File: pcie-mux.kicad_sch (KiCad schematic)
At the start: 50 parts, among them Q6 BSS138PW,115, Q7 BSS138PW,115, Q8 BSS138PW,115, SW1 SW_CVS-02B, U10 TMUXHS4412RUAR, U11 CBTL02043ABQ, U7 SY75602BTWL-TR, U8 74LVC1G157-Q100H_SOT457, U9 NTS0302JKZ

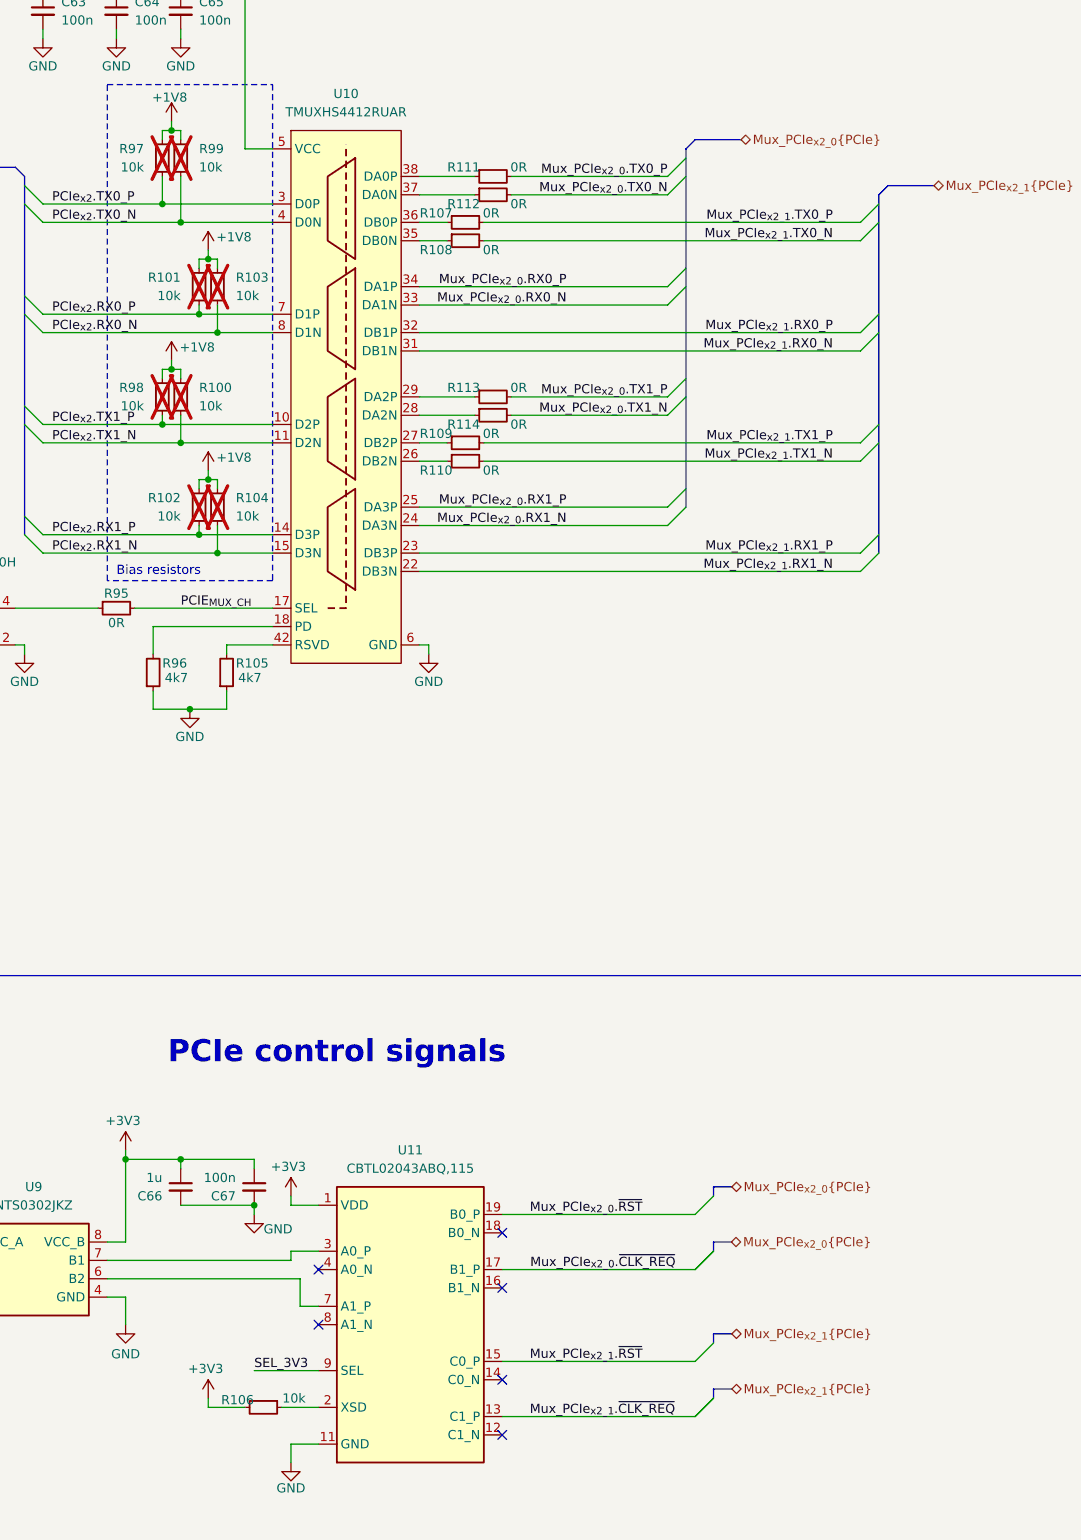
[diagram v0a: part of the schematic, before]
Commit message: [#100765] Prettify schematic
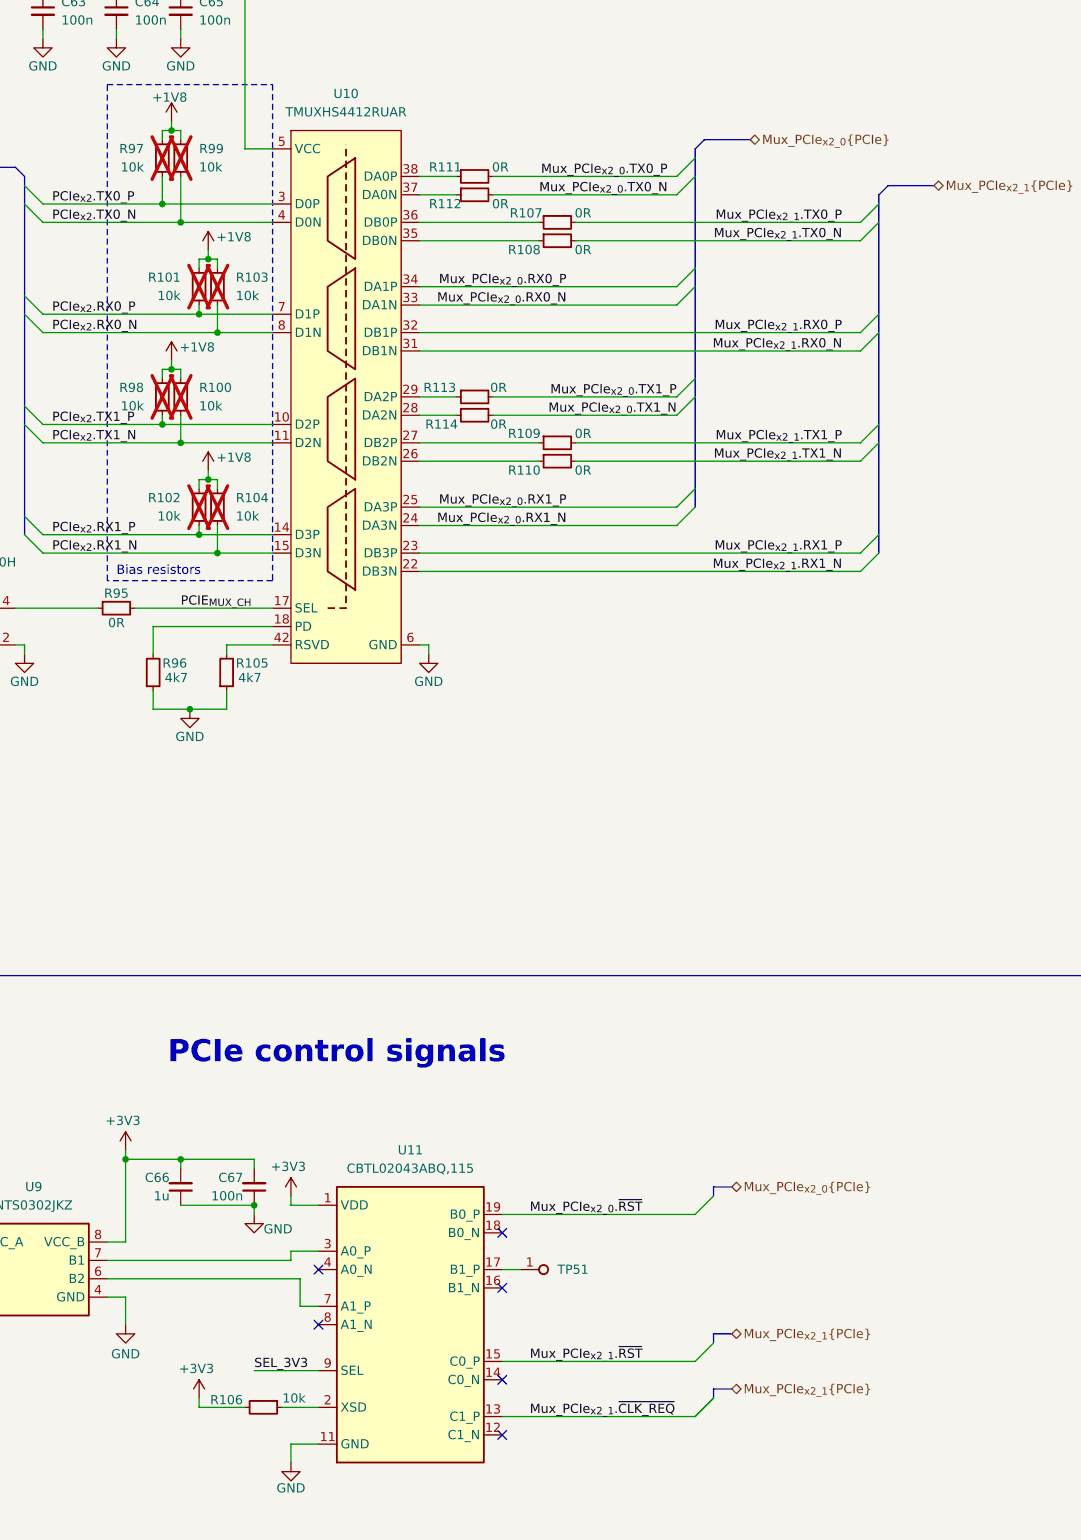
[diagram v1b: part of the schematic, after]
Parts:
- added TP51: TP_1mm_SMD, antmicro-footprints:TP_SMD_1mm, symbol antmicroTestPoints:TP_1mm_SMD
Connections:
- net +3V3: now also C66.2, C67.2; no longer C66.1, C67.1
- net GND: now also C66.1, C67.1; no longer C66.2, C67.2
- net Mux_PCIe_{x2_0}.~{CLK_REQ}: no longer names the net of U11.17 (B1_P)
- net Mux_PCIe_{x2_0}.~{CLK_REQ}: now also TP51.1
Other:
- moved on the sheet: R107, R108, R109, R110, R111, R112, R113, R114

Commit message: [#101557] Fix designator in status LED label
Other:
- note added: "D8: OFF, D9: ON = PORT A"
- note added: "D8: ON, D9: OFF = PORT B"
- note removed: "D6: OFF, D7: ON = PORT A"
- note removed: "D6: ON, D7: OFF = PORT B"
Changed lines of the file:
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@@
 		)
 	)
-	(text "D6: OFF, D7: ON = PORT A"
+	(text "D8: OFF, D9: ON = PORT A"
 		(exclude_from_sim no)
 		(at 107.188 211.074 0)
@@
 		)
 	)
-	(text "D6: ON, D7: OFF = PORT B"
+	(text "D8: ON, D9: OFF = PORT B"
 		(exclude_from_sim no)
 		(at 93.98 214.63 0)

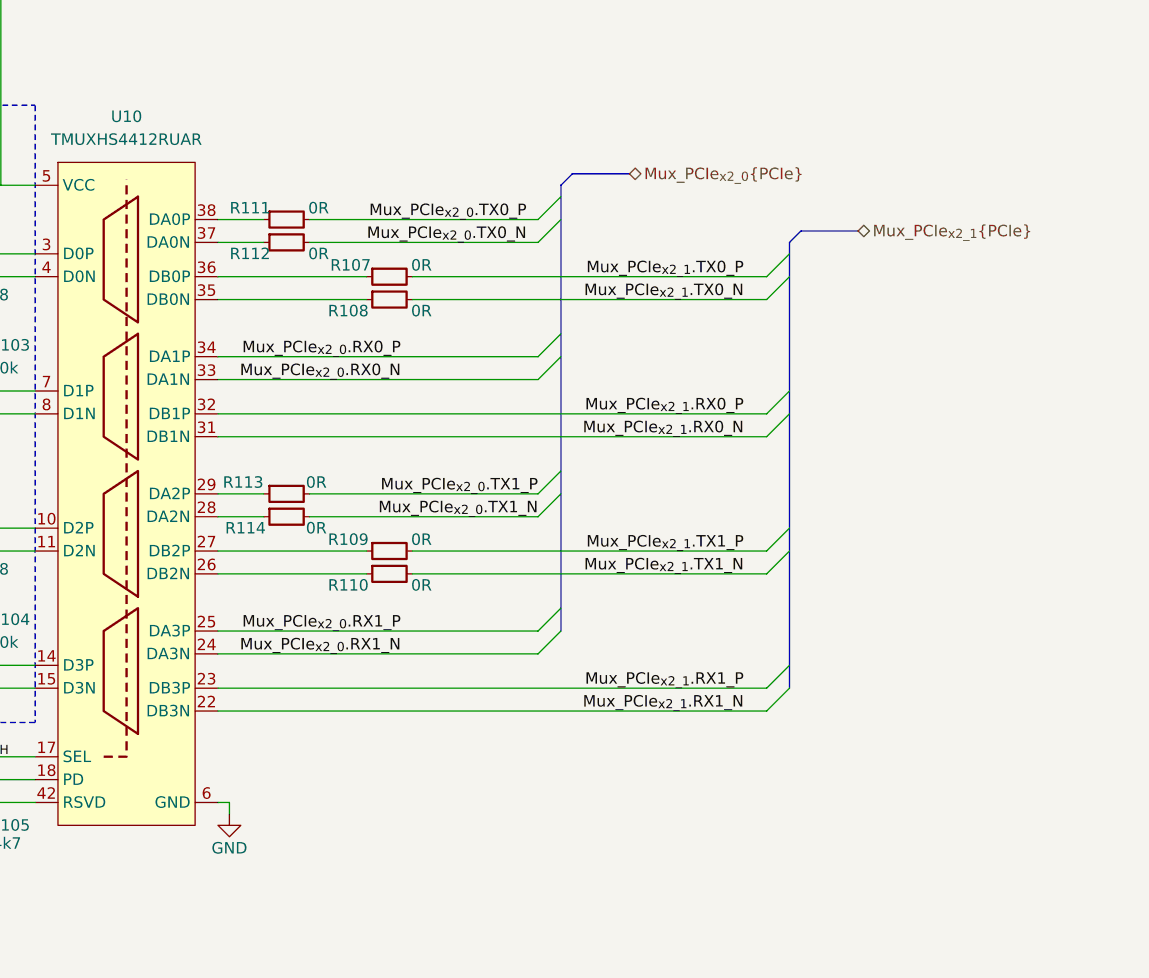
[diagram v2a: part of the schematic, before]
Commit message: [#101557] Add additional labels on HS lines
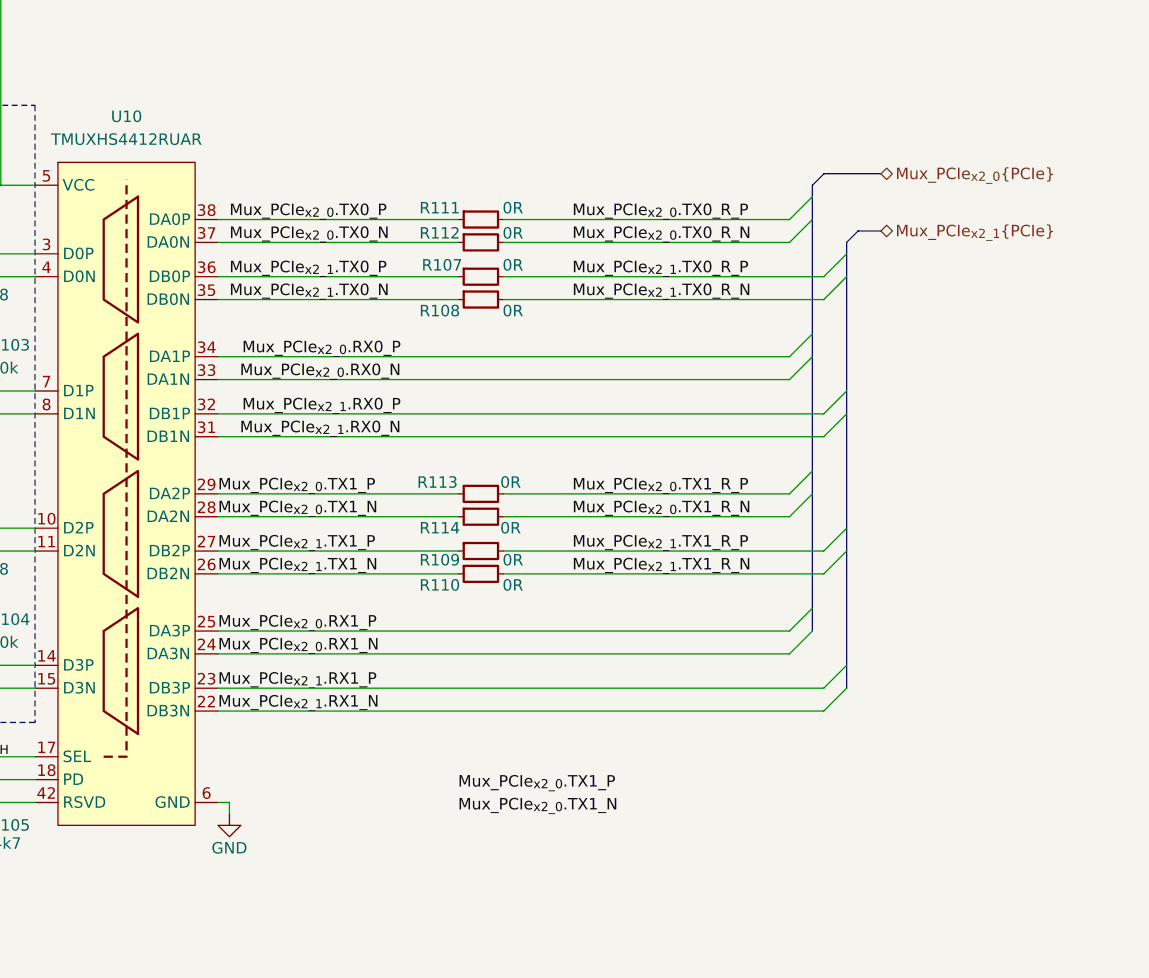
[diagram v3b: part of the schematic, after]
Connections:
- net Mux_PCIe_{x2_0}.TX0_N: now also R112.1, U10.37 (DA0N); no longer R112.2
- net Mux_PCIe_{x2_0}.TX0_P: now also R111.1, U10.38 (DA0P); no longer R111.2
- net Mux_PCIe_{x2_0}.TX1_N: now also R114.1, U10.28 (DA2N); no longer R114.2
- net Mux_PCIe_{x2_0}.TX1_P: now also R113.1, U10.29 (DA2P); no longer R113.2
- net Mux_PCIe_{x2_1}.TX0_N: now also R108.1, U10.35 (DB0N); no longer R108.2
- net Mux_PCIe_{x2_1}.TX0_P: now also R107.1, U10.36 (DB0P); no longer R107.2
- net Mux_PCIe_{x2_1}.TX1_N: now also R110.1, U10.26 (DB2N); no longer R110.2
- net Mux_PCIe_{x2_1}.TX1_P: now also R109.1, U10.27 (DB2P); no longer R109.2
- new net Mux_PCIe_{x2_0}.TX0_R_N: R112.2
- new net Mux_PCIe_{x2_0}.TX0_R_P: R111.2
- new net Mux_PCIe_{x2_0}.TX1_R_N: R114.2
- new net Mux_PCIe_{x2_0}.TX1_R_P: R113.2
- new net Mux_PCIe_{x2_1}.TX0_R_N: R108.2
- new net Mux_PCIe_{x2_1}.TX0_R_P: R107.2
- new net Mux_PCIe_{x2_1}.TX1_R_N: R110.2
- new net Mux_PCIe_{x2_1}.TX1_R_P: R109.2
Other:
- moved on the sheet: R107, R108, R109, R110, R111, R112, R113, R114

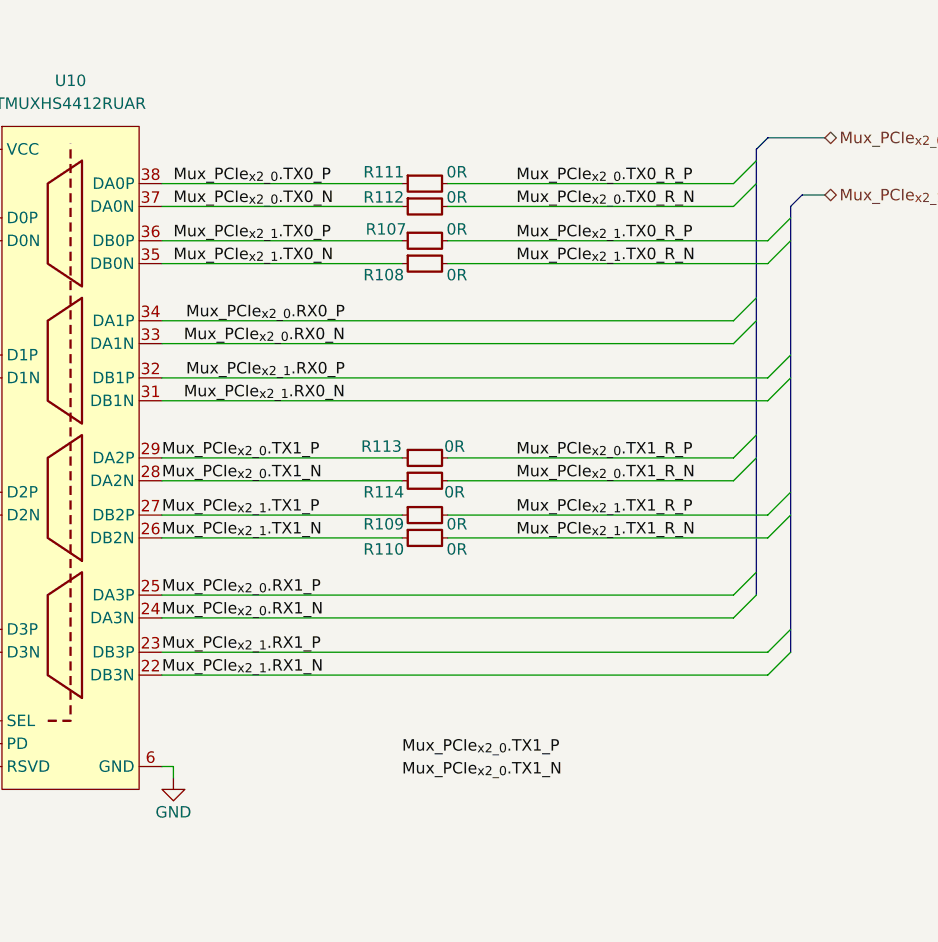
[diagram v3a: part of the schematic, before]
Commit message: [#101859] Add HS fanout from connectors
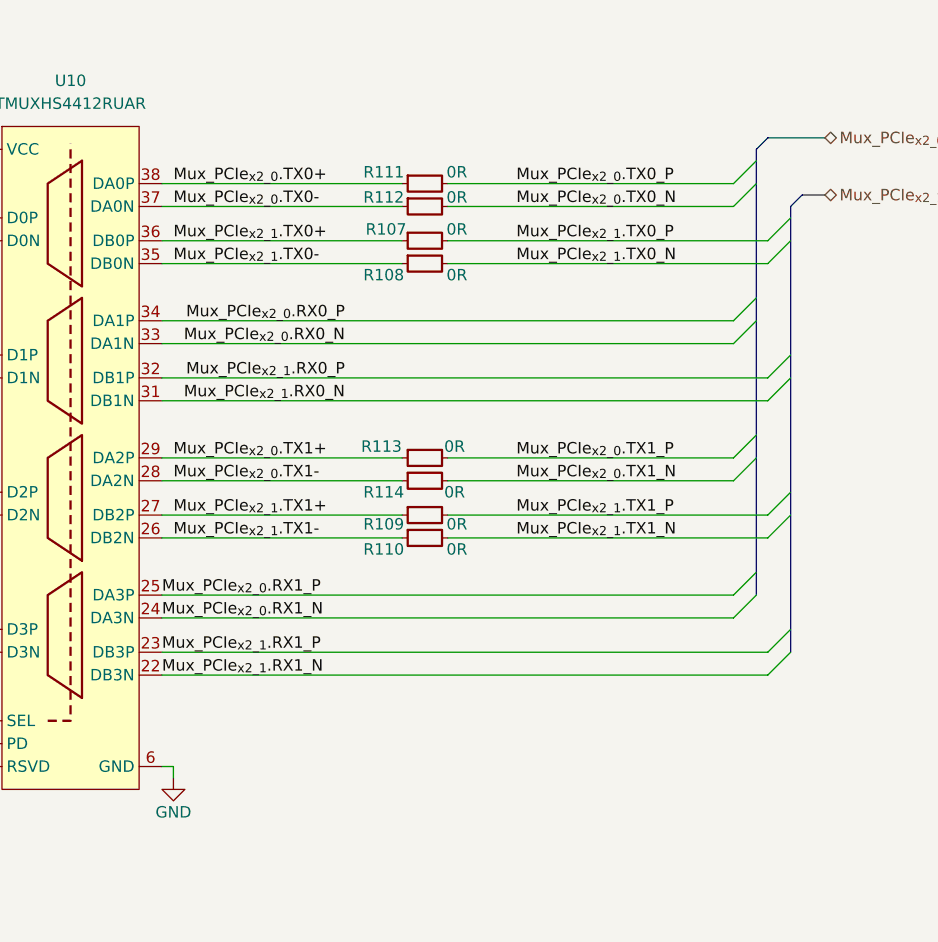
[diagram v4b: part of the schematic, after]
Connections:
- net Mux_PCIe_{x2_0}.TX0_R_N is gone; now on net Mux_PCIe_{x2_0}.TX0_N: R112.2
- net Mux_PCIe_{x2_0}.TX0_R_P is gone; now on net Mux_PCIe_{x2_0}.TX0_P: R111.2
- net Mux_PCIe_{x2_0}.TX1_R_N is gone; now on net Mux_PCIe_{x2_0}.TX1_N: R114.2
- net Mux_PCIe_{x2_0}.TX1_R_P is gone; now on net Mux_PCIe_{x2_0}.TX1_P: R113.2
- net Mux_PCIe_{x2_1}.TX0_R_N is gone; now on net Mux_PCIe_{x2_1}.TX0_N: R108.2
- net Mux_PCIe_{x2_1}.TX0_R_P is gone; now on net Mux_PCIe_{x2_1}.TX0_P: R107.2
- net Mux_PCIe_{x2_1}.TX1_R_N is gone; now on net Mux_PCIe_{x2_1}.TX1_N: R110.2
- net Mux_PCIe_{x2_1}.TX1_R_P is gone; now on net Mux_PCIe_{x2_1}.TX1_P: R109.2
- net Mux_PCIe_{x2_0}.TX0_N: no longer R112.1, U10.37 (DA0N)
- net Mux_PCIe_{x2_0}.TX0_P: no longer R111.1, U10.38 (DA0P)
- net Mux_PCIe_{x2_0}.TX1_N: no longer R114.1, U10.28 (DA2N)
- net Mux_PCIe_{x2_0}.TX1_P: no longer R113.1, U10.29 (DA2P)
- net Mux_PCIe_{x2_1}.TX0_N: no longer R108.1, U10.35 (DB0N)
- net Mux_PCIe_{x2_1}.TX0_P: no longer R107.1, U10.36 (DB0P)
- net Mux_PCIe_{x2_1}.TX1_N: no longer R110.1, U10.26 (DB2N)
- net Mux_PCIe_{x2_1}.TX1_P: no longer R109.1, U10.27 (DB2P)
- new net Mux_PCIe_{x2_0}.TX0+: R111.1, U10.38 (DA0P)
- new net Mux_PCIe_{x2_0}.TX0-: R112.1, U10.37 (DA0N)
- new net Mux_PCIe_{x2_0}.TX1+: R113.1, U10.29 (DA2P)
- new net Mux_PCIe_{x2_0}.TX1-: R114.1, U10.28 (DA2N)
- new net Mux_PCIe_{x2_1}.TX0+: R107.1, U10.36 (DB0P)
- new net Mux_PCIe_{x2_1}.TX0-: R108.1, U10.35 (DB0N)
- new net Mux_PCIe_{x2_1}.TX1+: R109.1, U10.27 (DB2P)
- new net Mux_PCIe_{x2_1}.TX1-: R110.1, U10.26 (DB2N)
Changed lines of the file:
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@@
-		)
-	)
-	(label "Mux_PCIe_{x2_0}.TX0_R_P"
-		(at 353.06 67.31 0)
-		(effects
-			(font
-				(size 1.27 1.27)
-			)
-			(justify left bottom)
 		)
 	)
@@
 		)
 	)
-	(label "Mux_PCIe_{x2_0}.TX1_P"
-		(at 340.36 130.81 0)
-		(effects
-			(font
-				(size 1.27 1.27)
-			)
-			(justify left bottom)
-		)
-	)
 	(label "Mux_PCIe_{x2_1}.TX1_N"
-		(at 313.69 106.68 0)
+		(at 353.06 106.68 0)
 		(effects
 			(font
@@
 		)
 	)
-	(label "Mux_PCIe_{x2_0}.TX0_R_N"
-		(at 353.06 69.85 0)
-		(effects
-			(font
-				(size 1.27 1.27)
-			)
-			(justify left bottom)
-		)
-	)
 	(label "Mux_PCIe_{x2_0}.RX0_N"
 		(at 334.01 85.09 180)
@@
 		)
 	)
+	(label "Mux_PCIe_{x2_1}.TX0+"
+		(at 314.96 73.66 0)
+		(effects
+			(font
+				(size 1.27 1.27)
+			)
+			(justify left bottom)
+		)
+	)
 	(label "PCIe_{x2}.~{RST}"
 		(at 220.98 217.17 180)
@@
 	)
 	(label "Mux_PCIe_{x2_0}.TX1_P"
-		(at 313.69 97.79 0)
+		(at 353.06 97.79 0)
 		(effects
 			(font
@@
 	)
 	(label "Mux_PCIe_{x2_1}.TX0_P"
-		(at 314.96 73.66 0)
+		(at 353.06 73.66 0)
 		(effects
 			(font
@@
 	)
 	(label "Mux_PCIe_{x2_1}.TX0_N"
-		(at 314.96 76.2 0)
+		(at 353.06 76.2 0)
 		(effects
 			(font
@@
 	)
 	(label "Mux_PCIe_{x2_0}.TX1_N"
-		(at 313.69 100.33 0)
+		(at 353.06 100.33 0)
 		(effects
 			(font
@@
 	)
 	(label "Mux_PCIe_{x2_0}.TX0_N"
-		(at 314.96 69.85 0)
+		(at 353.06 69.85 0)
 		(effects
 			(font
@@
 		)
 	)
+	(label "Mux_PCIe_{x2_0}.TX0+"
+		(at 314.96 67.31 0)
+		(effects
+			(font
+				(size 1.27 1.27)
+			)
+			(justify left bottom)
+		)
+	)
 	(label "PCIe_{x2}.TX1_P"
 		(at 262.89 101.6 0)
@@
 	)
 	(label "Mux_PCIe_{x2_1}.TX1_P"
-		(at 313.69 104.14 0)
+		(at 353.06 104.14 0)
 		(effects
 			(font
@@
 		)
 	)
-	(label "Mux_PCIe_{x2_1}.TX0_R_P"
-		(at 353.06 73.66 0)
-		(effects
-			(font
-				(size 1.27 1.27)
-			)
-			(justify left bottom)
-		)
-	)
 	(label "Mux_PCIe_{x2_1}.CLK_N"
 		(at 100.33 143.51 0)
@@
 		)
 	)
-	(label "Mux_PCIe_{x2_1}.TX1_R_P"
-		(at 353.06 104.14 0)
+	(label "Mux_PCIe_{x2_0}.TX1-"
+		(at 314.96 100.33 0)
 		(effects
 			(font
@@
 		)
 	)
-	(label "Mux_PCIe_{x2_0}.TX1_N"
-		(at 340.36 133.35 0)
-		(effects
-			(font
-				(size 1.27 1.27)
-			)
-			(justify left bottom)
-		)
-	)
-	(label "Mux_PCIe_{x2_0}.TX1_R_P"
-		(at 353.06 97.79 0)
-		(effects
-			(font
-				(size 1.27 1.27)
-			)
-			(justify left bottom)
-		)
-	)
-	(label "Mux_PCIe_{x2_1}.TX0_R_N"
-		(at 353.06 76.2 0)
-		(effects
-			(font
-				(size 1.27 1.27)
-			)
-			(justify left bottom)
-		)
-	)
 	(label "Mux_PCIe_{x2_1}.~{CLK_REQ}"
 		(at 328.93 238.76 0)
@@
 		)
 	)
-	(label "Mux_PCIe_{x2_0}.TX1_R_N"
-		(at 353.06 100.33 0)
+	(label "Mux_PCIe_{x2_1}.TX1-"
+		(at 314.96 106.68 0)
 		(effects
 			(font
@@
 		)
 	)
+	(label "Mux_PCIe_{x2_1}.TX0-"
+		(at 314.96 76.2 0)
+		(effects
+			(font
+				(size 1.27 1.27)
+			)
+			(justify left bottom)
+		)
+	)
 	(label "Mux_PCIe_{x2_0}.RX0_P"
 		(at 334.01 82.55 180)
@@
 		)
 	)
+	(label "Mux_PCIe_{x2_0}.TX1+"
+		(at 314.96 97.79 0)
+		(effects
+			(font
+				(size 1.27 1.27)
+			)
+			(justify left bottom)
+		)
+	)
+	(label "Mux_PCIe_{x2_0}.TX0-"
+		(at 314.96 69.85 0)
+		(effects
+			(font
+				(size 1.27 1.27)
+			)
+			(justify left bottom)
+		)
+	)
 	(label "Mux_PCIe_{x2_0}.~{RST}"
 		(at 328.93 210.82 0)
@@
 		)
 	)
-	(label "Mux_PCIe_{x2_1}.TX1_R_N"
-		(at 353.06 106.68 0)
-		(effects
-			(font
-				(size 1.27 1.27)
-			)
-			(justify left bottom)
-		)
-	)
 	(label "PCIe_{x2}.TX1_N"
 		(at 262.89 104.14 0)
@@
 		)
 	)
+	(label "Mux_PCIe_{x2_1}.TX1+"
+		(at 314.96 104.14 0)
+		(effects
+			(font
+				(size 1.27 1.27)
+			)
+			(justify left bottom)
+		)
+	)
 	(label "Mux_PCIe_{x2_0}.TX0_P"
-		(at 314.96 67.31 0)
-		(effects
-			(font
+		(at 353.06 67.31 0)
+		(effects
+			(font
